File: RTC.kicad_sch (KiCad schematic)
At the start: 5 parts

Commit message: Annotate schematic
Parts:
- removed Y?: Crystal_Small, symbol Device:Crystal_Small
- added C201: 0.01u, Capacitor_SMD:C_0402_1005Metric, symbol Device:C_Small
- added X201: ASE-xxxMHz, Oscillator:Oscillator_SMD_Abracon_ASE-4Pin_3.2x2.5mm, symbol Oscillator:ASE-xxxMHz
- BT201: renamed from BT?; footprint (none) -> Battery:BatteryHolder_MPD_BC2003_1x2032
- R201, R202: renamed from R?; footprint (none) -> Resistor_SMD:R_0402_1005Metric
- gave numbers to parts that had none: 1
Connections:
- net +3V3: now also C201.1, X201.1 (EN), X201.4 (Vdd)
- net GND: now also C201.2, X201.2 (GND)
- net REF_CLK: now reaches U201.1 (X1)
- net REF_CLK: now also X201.3 (OUT)
- no-connect marks 0 -> 1
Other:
- moved on the sheet: BT201, R201, R202, U201

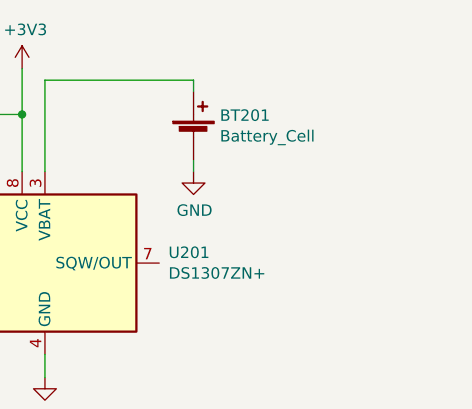
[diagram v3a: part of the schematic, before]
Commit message: Fix footprint associations, use 74LVC2G07 instead of MOSFETs
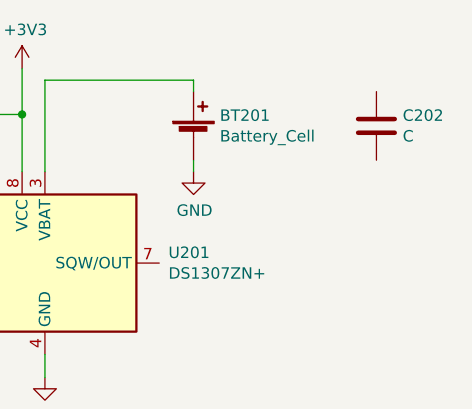
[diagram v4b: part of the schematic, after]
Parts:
- added C202: C, symbol Device:C
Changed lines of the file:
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@@
+    )
+  )
+  (symbol (lib_id "Device:C") (at 252.73 102.87 0) (unit 1)
+    (in_bom yes) (on_board yes)
+    (property "Reference" "C202" (id 0) (at 255.6511 101.7206 0)
+      (effects (font (size 1.27 1.27)) (justify left))
+    )
+    (property "Value" "C" (id 1) (at 255.6511 104.0193 0)
+      (effects (font (size 1.27 1.27)) (justify left))
+    )
+    (property "Footprint" "" (id 2) (at 253.6952 106.68 0)
+      (effects (font (size 1.27 1.27)) hide)
+    )
+    (property "Datasheet" "~" (id 3) (at 252.73 102.87 0)
+      (effects (font (size 1.27 1.27)) hide)
     )
   )

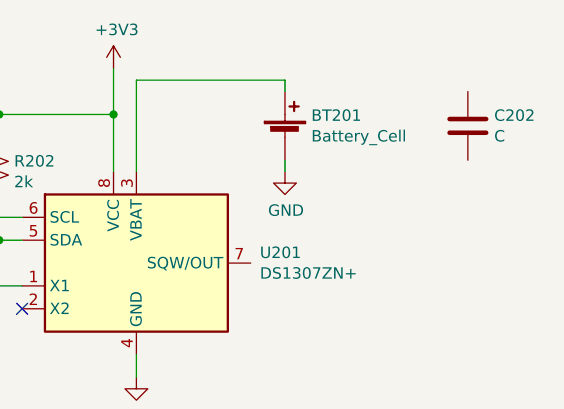
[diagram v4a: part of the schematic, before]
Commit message: Connect Ethernet and USB to MIO, start layout
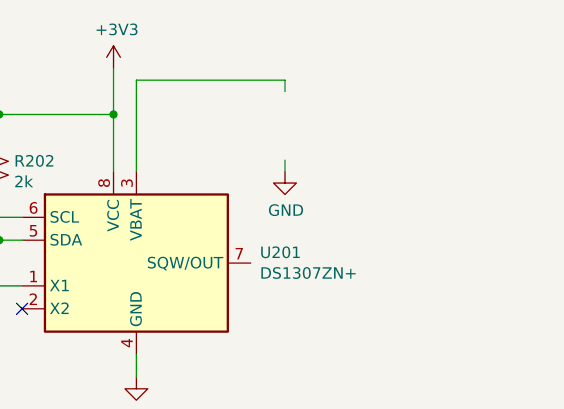
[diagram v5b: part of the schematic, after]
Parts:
- removed BT201: Battery_Cell, Battery:BatteryHolder_MPD_BC2003_1x2032, symbol Device:Battery_Cell
- removed C202: C, symbol Device:C
- C201: footprint Capacitor_SMD:C_0402_1005Metric -> Capacitor_SMD:C_0603_1608Metric
- R201, R202: footprint Resistor_SMD:R_0402_1005Metric -> Resistor_SMD:R_0603_1608Metric
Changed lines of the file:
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@@
       (effects (font (size 1.27 1.27)) (justify left))
     )
-    (property "Footprint" "Resistor_SMD:R_0402_1005Metric" (id 2) (at 191.77 107.95 0)
+    (property "Footprint" "Resistor_SMD:R_0603_1608Metric" (id 2) (at 191.77 107.95 0)
       (effects (font (size 1.27 1.27)) hide)
     )
@@
       (effects (font (size 1.27 1.27)) (justify left))
     )
-    (property "Footprint" "Resistor_SMD:R_0402_1005Metric" (id 2) (at 200.66 107.95 0)
+    (property "Footprint" "Resistor_SMD:R_0603_1608Metric" (id 2) (at 200.66 107.95 0)
       (effects (font (size 1.27 1.27)) hide)
     )
@@
       (effects (font (size 1.27 1.27)) (justify left))
     )
-    (property "Footprint" "Capacitor_SMD:C_0402_1005Metric" (id 2) (at 116.84 120.65 0)
+    (property "Footprint" "Capacitor_SMD:C_0603_1608Metric" (id 2) (at 116.84 120.65 0)
       (effects (font (size 1.27 1.27)) hide)
     )
@@
       (effects (font (size 1.27 1.27)) hide)
     )
-  )
-  (symbol (lib_id "Device:Battery_Cell") (at 232.41 104.14 0) (unit 1)
-    (in_bom yes) (on_board yes)
-    (property "Reference" "BT201" (id 0) (at 235.3311 101.7206 0)
-      (effects (font (size 1.27 1.27)) (justify left))
-    )
-    (property "Value" "Battery_Cell" (id 1) (at 235.3311 104.0193 0)
-      (effects (font (size 1.27 1.27)) (justify left))
-    )
-    (property "Footprint" "Battery:BatteryHolder_MPD_BC2003_1x2032" (id 2) (at 232.41 102.616 90)
-      (effects (font (size 1.27 1.27)) hide)
-    )
-    (property "Datasheet" "~" (id 3) (at 232.41 102.616 90)
-      (effects (font (size 1.27 1.27)) hide)
-    )
-  )
-  (symbol (lib_id "Device:C") (at 252.73 102.87 0) (unit 1)
-    (in_bom yes) (on_board yes)
-    (property "Reference" "C202" (id 0) (at 255.6511 101.7206 0)
-      (effects (font (size 1.27 1.27)) (justify left))
-    )
-    (property "Value" "C" (id 1) (at 255.6511 104.0193 0)
-      (effects (font (size 1.27 1.27)) (justify left))
-    )
-    (property "Footprint" "" (id 2) (at 253.6952 106.68 0)
-      (effects (font (size 1.27 1.27)) hide)
-    )
-    (property "Datasheet" "~" (id 3) (at 252.73 102.87 0)
-      (effects (font (size 1.27 1.27)) hide)
-    )

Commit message: Place motor drivers, start layout of Ethernet PHY
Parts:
- C201: footprint Capacitor_SMD:C_0603_1608Metric -> Capacitor_SMD:C_0402_1005Metric
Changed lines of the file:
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@@
-(kicad_sch (version 20200618) (host eeschema "5.99.0-unknown-77313e4~101~ubuntu20.04.1")
+(kicad_sch (version 20200618) (host eeschema "5.99.0-unknown-7340c97~102~ubuntu20.04.1")
   (page 2 14)
   (paper "B")
@@
       (effects (font (size 1.27 1.27)) (justify left))
     )
-    (property "Footprint" "Capacitor_SMD:C_0603_1608Metric" (id 2) (at 116.84 120.65 0)
-      (effects (font (size 1.27 1.27)) hide)
-    )
+    (property "Footprint" "Capacitor_SMD:C_0402_1005Metric" (id 2) (at 116.84 120.65 0)
+      (effects (font (size 1.27 1.27)) hide)
+    )
